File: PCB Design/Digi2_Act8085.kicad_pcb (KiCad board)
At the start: 2 copper layers, 27 parts, among them U1 8085A, U10 8255, U2 Barrel_Jack, U3 L7805, U4 2764, U5 CY6264, U6 74LS373, U7 74LS138, U8 8255, U9 8255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

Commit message: New Board Layout
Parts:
- C1, C11: footprint Capacitor_THT:CP_Radial_D8.0mm_P3.50mm -> Capacitor_THT:CP_Radial_D5.0mm_P2.50mm
- C10: footprint Capacitor_THT:CP_Radial_D8.0mm_P3.50mm -> Capacitor_THT:CP_Radial_D4.0mm_P2.00mm
- C12: footprint Capacitor_THT:CP_Radial_D8.0mm_P3.50mm -> Capacitor_THT:C_Disc_D4.3mm_W1.9mm_P5.00mm
- moved U2 169.8 mm to (42.5, 57.2)
- moved R1 161.6 mm to (46.7, 62.0)
- moved D2 152.5 mm to (47.4, 55.2)
- moved Y1 151.4 mm to (68.9, 87.8), turned to -90 degrees
- moved D1 147.4 mm to (63.0, 65.2), turned to 180 degrees
- moved FB1 141.1 mm to (50.5, 47.5), turned to 180 degrees
- moved U3 139.9 mm to (69.8, 55.2), turned to -90 degrees
- moved C10 135.8 mm to (55.2, 47.5)
- moved C11 129.7 mm to (61.2, 47.5)
- moved C12 127.8 mm to (68.9, 100.1), turned to -90 degrees
- moved C2 127.8 mm to (82.8, 83.4)
- moved C1 122.7 mm to (69.0, 47.5)
- moved C4 120.6 mm to (102.4, 109.3)
- moved U1 109.5 mm to (77.7, 88.1)
- moved C3 106.3 mm to (101.6, 76.3)
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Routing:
- net +5V: track 0.00 -> 1.88 mm

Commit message: Initial B
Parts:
- moved C5 43.9 mm to (168.1, 116.1)
- moved C6 43.9 mm to (196.7, 116.1)
- moved C9 43.9 mm to (156.5, 104.8)
- moved U4 43.9 mm to (192.3, 121.2)
- moved U5 43.9 mm to (162.8, 121.2)
- moved U8 43.9 mm to (161.0, 110.2)
- moved C7 40.7 mm to (156.4, 52.6)
- moved C8 40.7 mm to (156.4, 73.9)
- moved U10 40.7 mm to (160.9, 56.7)
- moved U9 40.7 mm to (160.8, 79.4)
- moved C2 27.5 mm to (66.6, 105.7)
- moved C3 27.5 mm to (85.4, 98.5)
- moved U1 27.5 mm to (61.5, 110.3)
- moved C12 27.5 mm to (52.7, 122.3)
- moved U7 27.5 mm to (84.1, 103.6)
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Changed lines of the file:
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@@
 	(footprint "Capacitor_THT:C_Disc_D4.3mm_W1.9mm_P5.00mm"
 		(layer "F.Cu")
-		(at 82.81 83.425)
+		(at 66.625 105.67)
 		(descr "C, Disc series, Radial, pin pitch=5.00mm, , diameter*width=4.3*1.9mm^2, Capacitor, http://www.vishay.com/docs/45233/krseries.pdf")
 		(tags "C Disc series Radial pin pitch 5.00mm  diameter 4.3mm width 1.9mm Capacitor")
@@
 	(footprint "Crystal:Crystal_HC49-U_Vertical"
 		(layer "F.Cu")
-		(at 68.925 87.795 -90)
+		(at 52.74 110.04 -90)
 		(descr "Crystal THT HC-49/U http://5hertz.com/pdfs/04404_D.pdf")
 		(tags "THT crystalHC-49/U")
@@
 	(footprint "Package_DIP:DIP-16_W7.62mm_Socket"
 		(layer "F.Cu")
-		(at 100.24 81.36)
+		(at 84.055 103.605)
 		(descr "16-lead though-hole mounted DIP package, row spacing 7.62 mm (300 mils), Socket")
 		(tags "THT DIP DIL PDIP 2.54mm 7.62mm 300mil Socket")
@@
 	(footprint "Package_DIP:DIP-20_W7.62mm_Socket"
 		(layer "F.Cu")
-		(at 100.79 113.27)
+		(at 84.605 135.515)
 		(descr "20-lead though-hole mounted DIP package, row spacing 7.62 mm (300 mils), Socket")
 		(tags "THT DIP DIL PDIP 2.54mm 7.62mm 300mil Socket")
 		(property "Reference" "U6"
-			(at 8.37 -2.72 360)
+			(at 8.37 -2.72 0)
 			(layer "F.SilkS")
 			(effects
@@
 		)
 		(property "Value" "74LS373"
-			(at 7.945 26.37 360)
+			(at 7.945 26.37 0)
 			(layer "F.Fab")
 			(effects
@@
 		)
 		(fp_text user "${REFERENCE}"
-			(at 7.945 12.61 360)
+			(at 7.945 12.61 0)
 			(layer "F.Fab")
 			(effects
@@
 	(footprint "Capacitor_THT:C_Disc_D4.3mm_W1.9mm_P5.00mm"
 		(layer "F.Cu")
-		(at 116.5 86.76 90)
+		(at 156.53 104.76 90)
 		(descr "C, Disc series, Radial, pin pitch=5.00mm, , diameter*width=4.3*1.9mm^2, Capacitor, http://www.vishay.com/docs/45233/krseries.pdf")
 		(tags "C Disc series Radial pin pitch 5.00mm  diameter 4.3mm width 1.9mm Capacitor")
 		(property "Reference" "C9"
-			(at 2.5 -2.2 270)
+			(at 2.5 -2.2 -90)
 			(layer "F.SilkS")
 			(effects
@@
 		)
 		(property "Value" "100nF"
-			(at 2.5 2.2 270)
+			(at 2.5 2.2 -90)
 			(layer "F.Fab")
 			(effects
@@
 		)
 		(fp_text user "${REFERENCE}"
-			(at 2.5 0 270)
+			(at 2.5 0 -90)
 			(layer "F.Fab")
 			(effects
@@
 	(footprint "Package_DIP:DIP-40_W15.24mm"
 		(layer "F.Cu")
-		(at 121.085 48.615 90)
+		(at 160.92 56.74 90)
 		(descr "40-lead though-hole mounted DIP package, row spacing 15.24 mm (600 mils)")
 		(tags "THT DIP DIL PDIP 2.54mm 15.24mm 600mil")
 		(property "Reference" "U10"
-			(at 7.62 -2.33 270)
+			(at 7.62 -2.33 -90)
 			(layer "F.SilkS")
 			(effects
@@
 		)
 		(property "Value" "8255"
-			(at 7.62 50.59 270)
+			(at 7.62 50.59 -90)
 			(layer "F.Fab")
 			(effects
@@
 		)
 		(fp_text user "${REFERENCE}"
-			(at 7.62 24.13 270)
+			(at 7.62 24.13 -90)
 			(layer "F.Fab")
 			(effects
@@
 	(footprint "Capacitor_THT:C_Disc_D4.3mm_W1.9mm_P5.00mm"
 		(layer "F.Cu")
-		(at 101.61 76.27)
+		(at 85.425 98.515)
 		(descr "C, Disc series, Radial, pin pitch=5.00mm, , diameter*width=4.3*1.9mm^2, Capacitor, http://www.vishay.com/docs/45233/krseries.pdf")
 		(tags "C Disc series Radial pin pitch 5.00mm  diameter 4.3mm width 1.9mm Capacitor")
@@
 	(footprint "Package_DIP:DIP-28_W15.24mm_Socket"
 		(layer "F.Cu")
-		(at 122.82 103.225)
+		(at 162.85 121.225)
 		(descr "28-lead though-hole mounted DIP package, row spacing 15.24 mm (600 mils), Socket")
 		(tags "THT DIP DIL PDIP 2.54mm 15.24mm 600mil Socket")
@@
 	(footprint "Package_DIP:DIP-28_W15.24mm"
 		(layer "F.Cu")
-		(at 152.3 103.19)
+		(at 192.33 121.19)
 		(descr "28-lead though-hole mounted DIP package, row spacing 15.24 mm (600 mils)")
 		(tags "THT DIP DIL PDIP 2.54mm 15.24mm 600mil")
@@
 	(footprint "Capacitor_THT:C_Disc_D4.3mm_W1.9mm_P5.00mm"
 		(layer "F.Cu")
-		(at 116.54 65.76 90)
+		(at 156.375 73.885 90)
 		(descr "C, Disc series, Radial, pin pitch=5.00mm, , diameter*width=4.3*1.9mm^2, Capacitor, http://www.vishay.com/docs/45233/krseries.pdf")
 		(tags "C Disc series Radial pin pitch 5.00mm  diameter 4.3mm width 1.9mm Capacitor")
 		(property "Reference" "C8"
-			(at 2.5 -2.2 270)
+			(at 2.5 -2.2 -90)
 			(layer "F.SilkS")
 			(effects
@@
 		)
 		(property "Value" "100nF"
-			(at 2.5 2.2 270)
+			(at 2.5 2.2 -90)
 			(layer "F.Fab")
 			(effects
@@
 		)
 		(fp_text user "${REFERENCE}"
-			(at 2.5 0 270)
+			(at 2.5 0 -90)
 			(layer "F.Fab")
 			(effects
@@
 	(footprint "Capacitor_THT:C_Disc_D4.3mm_W1.9mm_P5.00mm"
 		(layer "F.Cu")
-		(at 128.06 98.07)
+		(at 168.09 116.07)
 		(descr "C, Disc series, Radial, pin pitch=5.00mm, , diameter*width=4.3*1.9mm^2, Capacitor, http://www.vishay.com/docs/45233/krseries.pdf")
 		(tags "C Disc series Radial pin pitch 5.00mm  diameter 4.3mm width 1.9mm Capacitor")
@@
 	(footprint "Package_DIP:DIP-40_W15.24mm"
 		(layer "F.Cu")
-		(at 77.685 88.095)
+		(at 61.5 110.34)
 		(descr "40-lead though-hole mounted DIP package, row spacing 15.24 mm (600 mils)")
 		(tags "THT DIP DIL PDIP 2.54mm 15.24mm 600mil")
@@
 	(footprint "Package_DIP:DIP-40_W15.24mm"
 		(layer "F.Cu")
-		(at 120.94 92.25 90)
+		(at 160.97 110.25 90)
 		(descr "40-lead though-hole mounted DIP package, row spacing 15.24 mm (600 mils)")
 		(tags "THT DIP DIL PDIP 2.54mm 15.24mm 600mil")
 		(property "Reference" "U8"
-			(at 7.62 -2.44 270)
+			(at 7.62 -2.44 -90)
 			(layer "F.SilkS")
 			(effects
@@
 		)
 		(property "Value" "8255"
-			(at 7.62 50.59 270)
+			(at 7.62 50.59 -90)
 			(layer "F.Fab")
 			(effects
@@
 		)
 		(fp_text user "${REFERENCE}"
-			(at 7.62 24.13 270)
+			(at 7.62 24.13 -90)
 			(layer "F.Fab")
 			(effects
@@
 	(footprint "Capacitor_THT:C_Disc_D4.3mm_W1.9mm_P5.00mm"
 		(layer "F.Cu")
-		(at 68.925 100.092349 -90)
+		(at 52.74 122.337349 -90)
 		(descr "C, Disc series, Radial, pin pitch=5.00mm, , diameter*width=4.3*1.9mm^2, Capacitor, http://www.vishay.com/docs/45233/krseries.pdf")
 		(tags "C Disc series Radial pin pitch 5.00mm  diameter 4.3mm width 1.9mm Capacitor")
@@
 	(footprint "Package_DIP:DIP-40_W15.24mm"
 		(layer "F.Cu")
-		(at 120.99 71.25 90)
+		(at 160.825 79.375 90)
 		(descr "40-lead though-hole mounted DIP package, row spacing 15.24 mm (600 mils)")
 		(tags "THT DIP DIL PDIP 2.54mm 15.24mm 600mil")
 		(property "Reference" "U9"
-			(at 7.62 -2.33 270)
+			(at 7.62 -2.33 -90)
 			(layer "F.SilkS")
 			(effects
@@
 		)
 		(property "Value" "8255"
-			(at 7.62 50.59 270)
+			(at 7.62 50.59 -90)
 			(layer "F.Fab")
 			(effects
@@
 		)
 		(fp_text user "${REFERENCE}"
-			(at 7.62 24.13 270)
+			(at 7.62 24.13 -90)
 			(layer "F.Fab")
 			(effects
@@
 	(footprint "Capacitor_THT:C_Disc_D4.3mm_W1.9mm_P5.00mm"
 		(layer "F.Cu")
-		(at 102.41 109.3)
+		(at 86.225 131.545)
 		(descr "C, Disc series, Radial, pin pitch=5.00mm, , diameter*width=4.3*1.9mm^2, Capacitor, http://www.vishay.com/docs/45233/krseries.pdf")
 		(tags "C Disc series Radial pin pitch 5.00mm  diameter 4.3mm width 1.9mm Capacitor")
 		(property "Reference" "C4"
-			(at 2.18 -5.355 360)
+			(at 2.18 -5.355 0)
 			(layer "F.SilkS")
 			(effects
@@
 		)
 		(property "Value" "100nF"
-			(at 2.5 2.2 360)
+			(at 2.5 2.2 0)
 			(layer "F.Fab")
 			(effects
@@
 		)
 		(fp_text user "${REFERENCE}"
-			(at 2.5 0 360)
+			(at 2.5 0 0)
 			(layer "F.Fab")
 			(effects
@@
 	(footprint "Capacitor_THT:C_Disc_D4.3mm_W1.9mm_P5.00mm"
 		(layer "F.Cu")
-		(at 156.675 98.115)
+		(at 196.705 116.115)
 		(descr "C, Disc series, Radial, pin pitch=5.00mm, , diameter*width=4.3*1.9mm^2, Capacitor, http://www.vishay.com/docs/45233/krseries.pdf")
 		(tags "C Disc series Radial pin pitch 5.00mm  diameter 4.3mm width 1.9mm Capacitor")
@@
 	(footprint "Capacitor_THT:C_Disc_D4.3mm_W1.9mm_P5.00mm"
 		(layer "F.Cu")
-		(at 116.54 44.51 90)
+		(at 156.375 52.635 90)
 		(descr "C, Disc series, Radial, pin pitch=5.00mm, , diameter*width=4.3*1.9mm^2, Capacitor, http://www.vishay.com/docs/45233/krseries.pdf")
 		(tags "C Disc series Radial pin pitch 5.00mm  diameter 4.3mm width 1.9mm Capacitor")
 		(property "Reference" "C7"
-			(at 2.5 -2.55 270)
+			(at 2.5 -2.55 -90)
 			(layer "F.SilkS")
 			(effects
@@
 		)
 		(property "Value" "100nF"
-			(at 2.5 2.2 270)
+			(at 2.5 2.2 -90)
 			(layer "F.Fab")
 			(effects
@@
 		)
 		(fp_text user "${REFERENCE}"
-			(at 2.5 0 270)
+			(at 2.5 0 -90)
 			(layer "F.Fab")
 			(effects
@@
 	)
 	(segment
-		(start 92.925 88.095)
-		(end 94.255 89.425)
+		(start 76.74 110.34)
+		(end 78.07 111.67)
 		(width 0.2)
 		(layer "F.Cu")

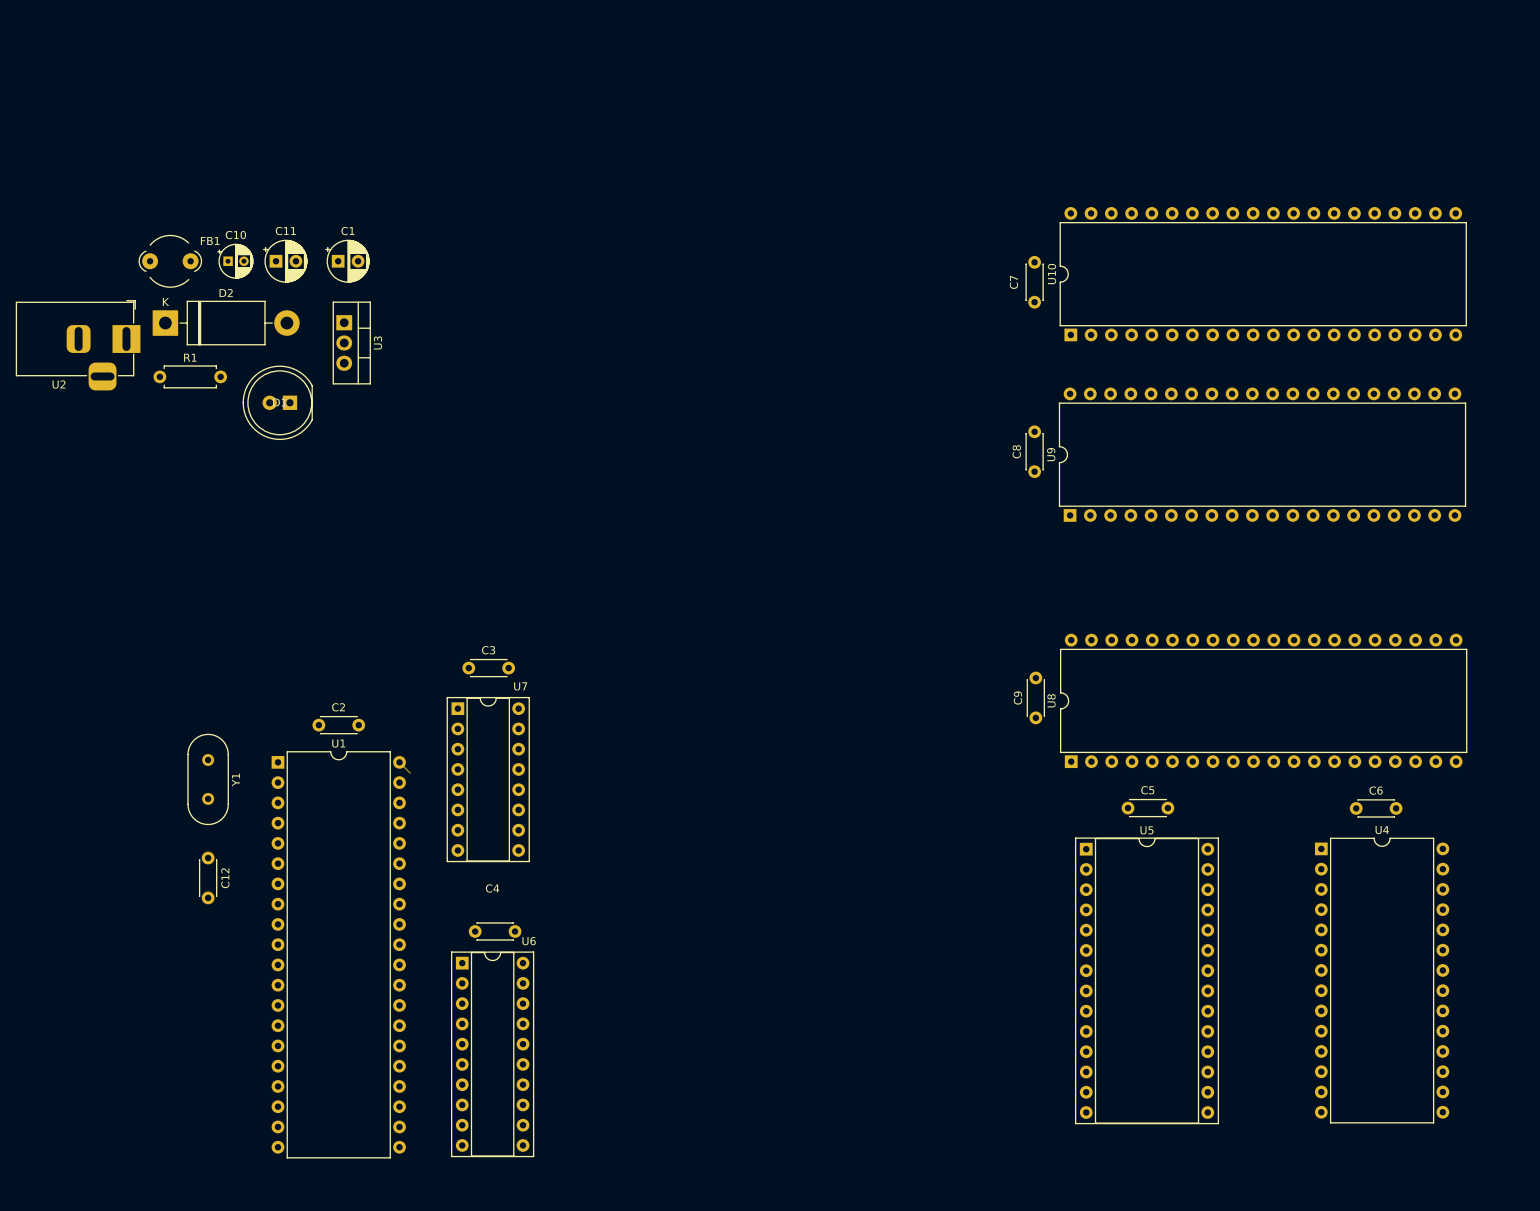
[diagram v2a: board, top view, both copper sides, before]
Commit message: Route 8085->Multiplexer
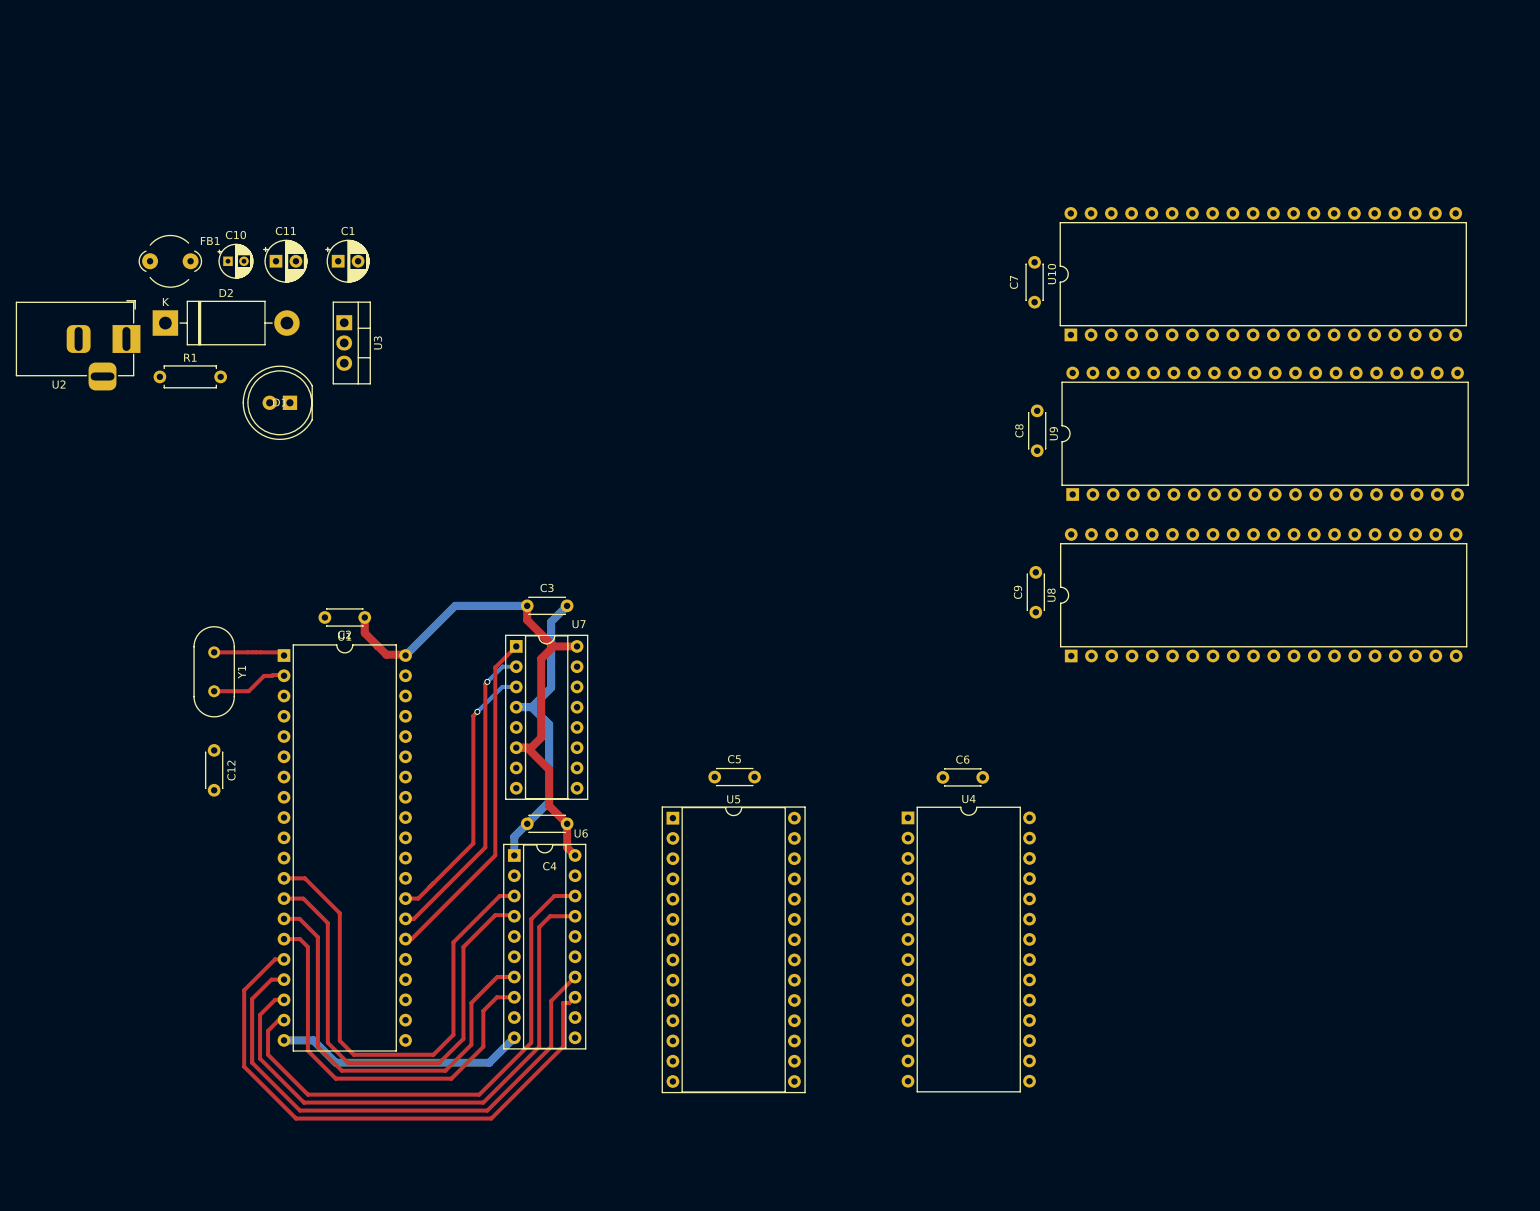
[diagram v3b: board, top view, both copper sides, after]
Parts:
- moved C6 52.0 mm to (144.9, 112.2)
- moved U4 52.0 mm to (140.5, 117.3)
- moved C5 52.0 mm to (116.3, 112.2)
- moved U5 52.0 mm to (111.0, 117.3)
- moved C4 17.8 mm to (97.8, 118.0), turned to 180 degrees
- moved U6 15.0 mm to (91.1, 122.0)
- moved C2 14.7 mm to (72.4, 92.2), turned to 180 degrees
- moved C12 13.5 mm to (53.5, 108.8)
- moved Y1 13.5 mm to (53.5, 96.5)
- moved U1 13.4 mm to (62.3, 96.9)
- moved C9 13.2 mm to (156.5, 91.5)
- moved U8 13.2 mm to (161.0, 97.0)
- moved C3 10.7 mm to (92.8, 90.7)
- moved U7 10.7 mm to (91.4, 95.8)
- moved U9 2.65 mm to (161.2, 76.8)
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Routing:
- net /Memory and Peripheral Inteface/AD4: track 0.00 -> 69.9 mm
- net /Memory and Peripheral Inteface/AD6: track 0.00 -> 69.5 mm
- net GND: track 0.00 -> 69.4 mm
- net +5V: track 1.88 -> 68.5 mm
- net /Memory and Peripheral Inteface/AD5: track 0.00 -> 66.3 mm
- net /Memory and Peripheral Inteface/AD7: track 0.00 -> 65.5 mm
- net /Memory and Peripheral Inteface/AD0: track 0.00 -> 62.5 mm
- net /Memory and Peripheral Inteface/AD1: track 0.00 -> 60.7 mm
- net /Memory and Peripheral Inteface/AD2: track 0.00 -> 52.8 mm
- net /Memory and Peripheral Inteface/AD3: track 0.00 -> 50.6 mm
- net /Memory and Peripheral Inteface/A13: track 0.00 -> 42.9 mm
- net /Memory and Peripheral Inteface/A14: track 0.00 -> 39.0 mm, vias 0 -> 1
- net /Memory and Peripheral Inteface/A15: track 0.00 -> 35.0 mm, vias 0 -> 1
- net Net-(C12-+): track 0.00 -> 9.60 mm
- net Net-(U1-X1): track 0.00 -> 8.88 mm

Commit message: Peripheral Routing
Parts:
- moved C7 18.8 mm to (156.5, 33.9), turned to -90 degrees
- moved U10 13.8 mm to (161.0, 43.0)
- moved C8 11.8 mm to (156.5, 59.5), turned to -90 degrees
- moved U9 6.75 mm to (161.0, 70.0)
- moved C9 5.00 mm to (156.5, 86.5), turned to -90 degrees
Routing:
- net +5V: track 68.5 -> 288.2 mm
- net GND: track 69.4 -> 195.2 mm
- net /Memory and Peripheral Inteface/AD3: track 50.6 -> 144.3 mm
- net /Memory and Peripheral Inteface/AD2: track 52.8 -> 142.5 mm
- net /Memory and Peripheral Inteface/AD1: track 60.7 -> 149.2 mm
- net /Memory and Peripheral Inteface/AD0: track 62.5 -> 148.9 mm
- net /Memory and Peripheral Inteface/~{WR}: track 0.00 -> 77.4 mm
- net /Memory and Peripheral Inteface/AD4: track 69.9 -> 145.3 mm
- net /Memory and Peripheral Inteface/AD5: track 66.3 -> 139.3 mm
- net /Memory and Peripheral Inteface/AD6: track 69.5 -> 139.6 mm
- net /Memory and Peripheral Inteface/AD7: track 65.5 -> 132.7 mm

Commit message: Additional Route
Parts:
- moved C7 33.0 mm to (123.9, 28.4)
- moved C8 33.0 mm to (124.0, 54.0)
- moved C9 33.0 mm to (124.0, 81.0)
- moved U10 33.0 mm to (128.5, 37.5)
- moved U8 33.0 mm to (128.4, 91.5)
- moved U9 33.0 mm to (128.4, 64.5)
- moved C5 7.11 mm to (121.2, 107.0), turned to 180 degrees
- moved C6 6.23 mm to (143.1, 106.3)
- moved U4 6.23 mm to (138.7, 111.3)
- moved U5 5.99 mm to (111.7, 111.4)
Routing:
- net /Memory and Peripheral Inteface/AD1: track 149.2 -> 302.6 mm, vias 0 -> 3
- net GND: track 195.2 -> 347.7 mm, vias 0 -> 5
- net /Memory and Peripheral Inteface/AD2: track 142.5 -> 287.0 mm, vias 0 -> 1
- net /Memory and Peripheral Inteface/A12: track 0.00 -> 135.9 mm, vias 0 -> 1
- net /Memory and Peripheral Inteface/A0: track 0.00 -> 103.3 mm
- net /Memory and Peripheral Inteface/~{WR}: track 77.4 -> 178.2 mm, vias 0 -> 1
- net /Memory and Peripheral Inteface/AD3: track 144.3 -> 243.2 mm, vias 0 -> 1
- net /Memory and Peripheral Inteface/A8: track 0.00 -> 96.8 mm
- net /Memory and Peripheral Inteface/A2: track 0.00 -> 94.8 mm, vias 0 -> 1
- net /Memory and Peripheral Inteface/A3: track 0.00 -> 94.7 mm, vias 0 -> 1
- net /Memory and Peripheral Inteface/A9: track 0.00 -> 91.4 mm
- net /Memory and Peripheral Inteface/~{RD}: track 0.00 -> 90.5 mm, vias 0 -> 1
- net /Memory and Peripheral Inteface/A1: track 0.00 -> 89.4 mm
- net /Memory and Peripheral Inteface/A11: track 0.00 -> 82.8 mm, vias 0 -> 1
- net /Memory and Peripheral Inteface/AD0: track 148.9 -> 231.6 mm, vias 0 -> 2
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
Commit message: updated p
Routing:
- net /Memory and Peripheral Inteface/A1: track 89.4 -> 307.6 mm, vias 0 -> 2
- net /Memory and Peripheral Inteface/A2: track 94.8 -> 307.2 mm, vias 1 -> 3
- net /Memory and Peripheral Inteface/~{RD}: track 90.5 -> 268.4 mm, vias 1 -> 2
- net /Memory and Peripheral Inteface/AD0: track 231.6 -> 363.6 mm
- net /Memory and Peripheral Inteface/~{Y4}: track 0.00 -> 100.5 mm, vias 0 -> 1
- net /Memory and Peripheral Inteface/~{WR}: track 178.2 -> 263.1 mm, vias 1 -> 2
- net /Memory and Peripheral Inteface/AD4: track 181.6 -> 253.2 mm
- net /Memory and Peripheral Inteface/AD5: track 175.7 -> 246.6 mm
- net /Memory and Peripheral Inteface/AD6: track 199.8 -> 267.8 mm
- net GND: track 347.7 -> 411.6 mm
- net /Memory and Peripheral Inteface/AD7: track 191.6 -> 253.1 mm
- net /Memory and Peripheral Inteface/AD3: track 243.2 -> 301.2 mm
- net /Memory and Peripheral Inteface/AD2: track 287.0 -> 343.7 mm
- net /Memory and Peripheral Inteface/AD1: track 302.6 -> 356.8 mm
- net +5V: track 314.8 -> 357.3 mm
